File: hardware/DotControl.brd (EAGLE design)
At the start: 30.7 x 65 mm, 42 parts, among them CN1 1X4-BIG, J3 USB-MICROB, SW2 Previous, SW5 Previous, SW6 Next, SW8 Ok, U1 ATMEGA328P-MU-QFN32, U2 TMP102, U3 ATSHA204-TSU, U4 SI7021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

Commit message: Readjust R values for charger, add Spice link
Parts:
- R1: value 10Ω -> 75Ω
- R6: value 70Ω -> 1kΩ
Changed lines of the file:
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@@
 <element name="CN1" library="adafruit" package="1X04-BIG" value="1X4-BIG" x="11.2" y="9"/>
 <element name="SJ1" library="SparkFun" package="SJ_2S-TRACE" value="SOLDERJUMPERTRACE" x="16.7" y="26.4" rot="MR90"/>
-<element name="R1" library="resistor" package="R0603" value="10Ω" x="28.4226" y="60.5282" rot="MR270"/>
+<element name="R1" library="resistor" package="R0603" value="75Ω" x="28.4226" y="60.5282" rot="MR270"/>
 <element name="LED2" library="SparkFun" package="LED-0603" value="" x="27.4828" y="60.6044" rot="R180"/>
 <element name="U2" library="SparkFun" package="SOT563" value="TMP102" x="18.9992" y="13.1318" rot="MR270"/>
@@
 <element name="C8" library="resistor" package="C0603" value="0.1uF" x="9.8552" y="19.3548" rot="MR90"/>
 <element name="C4" library="resistor" package="C0603" value="0.1uF" x="3.1242" y="17.6022" rot="MR270"/>
-<element name="R6" library="resistor" package="R0603" value="70Ω" x="23.876" y="61.3918" rot="MR0"/>
+<element name="R6" library="resistor" package="R0603" value="1kΩ" x="23.876" y="61.3918" rot="MR0"/>
 <element name="C5" library="adafruit" package="C3216" value="100uF 4V" x="5.4864" y="21.0312" rot="R180"/>
 </elements>

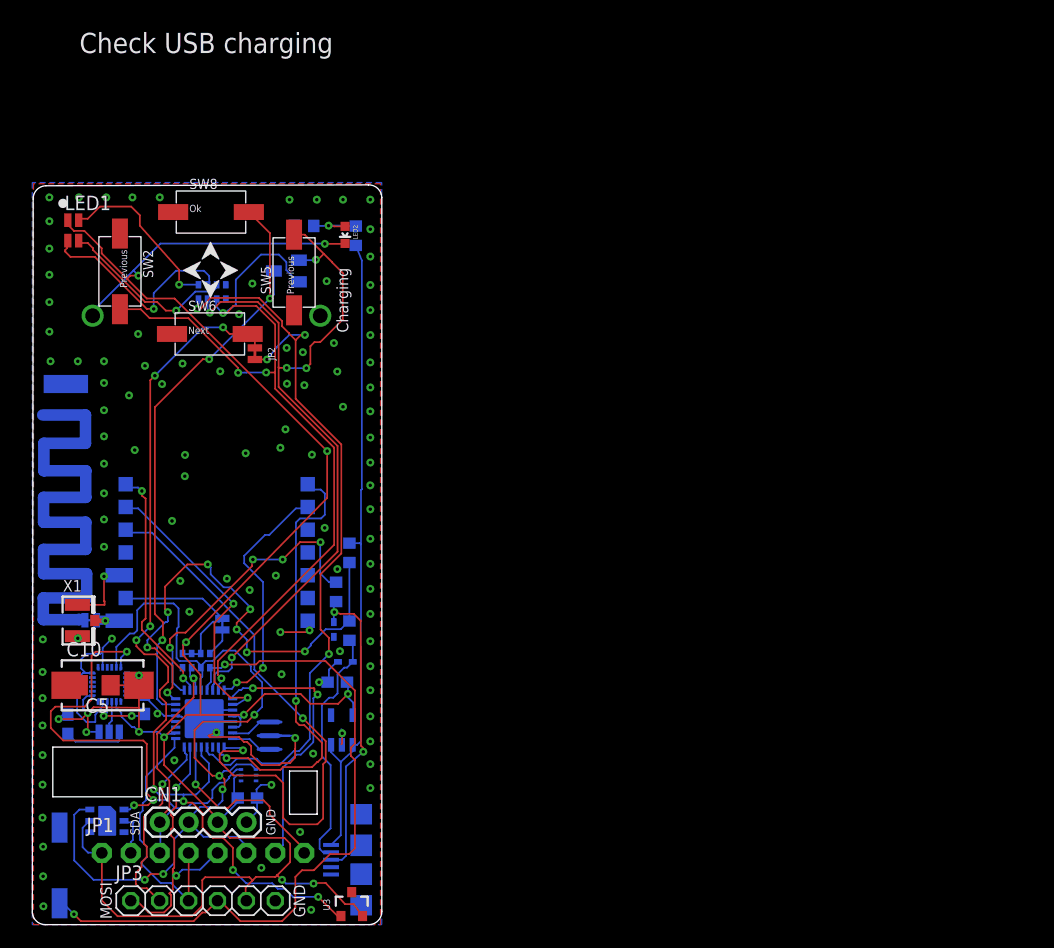
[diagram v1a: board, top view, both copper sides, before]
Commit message: Add pulldown on ENA pin of voltage reg to prefent 150uA quiescent current
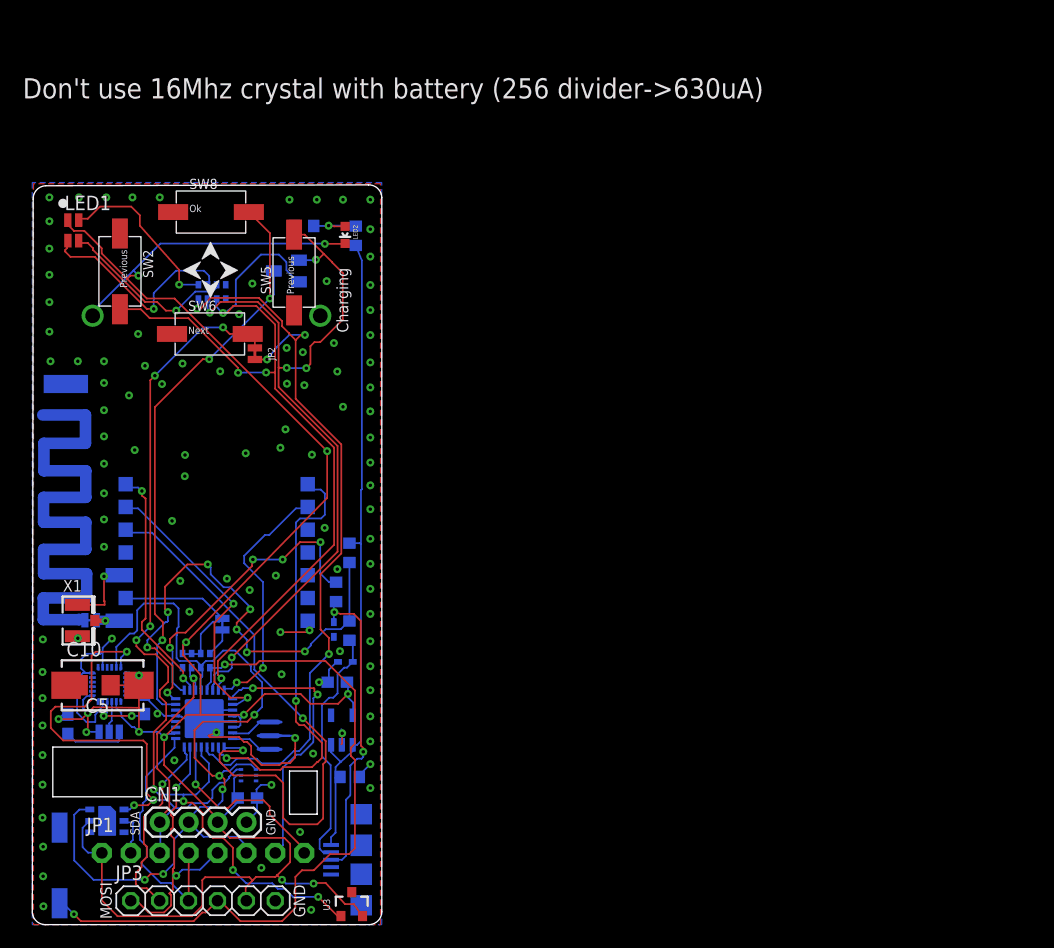
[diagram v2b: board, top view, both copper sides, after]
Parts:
- added R8: >1KΩ, resistor:R0603
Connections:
- net +5V: now also R8.2
- net GND: now also R8.1
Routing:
- net GND: track 79.4 -> 81.0 mm
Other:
- board text added: "Don't use 16Mhz crystal with battery (256 divider->630uA)"
- board text removed: "Check USB charging"
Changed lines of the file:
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@@
 <layer number="22" name="bPlace" color="7" fill="1" visible="yes" active="yes"/>
 <layer number="23" name="tOrigins" color="15" fill="1" visible="no" active="yes"/>
-<layer number="24" name="bOrigins" color="15" fill="1" visible="no" active="yes"/>
+<layer number="24" name="bOrigins" color="15" fill="1" visible="yes" active="yes"/>
 <layer number="25" name="tNames" color="7" fill="1" visible="no" active="yes"/>
 <layer number="26" name="bNames" color="7" fill="1" visible="no" active="yes"/>
@@
 <rectangle x1="0.1524" y1="25.527" x2="5.6388" y2="48.9204" layer="41"/>
 <rectangle x1="0.1524" y1="25.527" x2="5.6134" y2="48.9712" layer="42"/>
-<text x="4.1402" y="76.581" size="1.778" layer="21">Check USB charging</text>
 <text x="9.4234" y="7.8486" size="0.8128" layer="21" rot="R90">SDA</text>
 <text x="20.5486" y="10.16" size="0.8128" layer="21" rot="R270">GND</text>
+<text x="-0.8382" y="72.5932" size="1.778" layer="21">Don't use 16Mhz crystal with battery (256 divider-&gt;630uA)</text>
 </plain>
 <attributes>
@@
 <element name="R6" library="resistor" package="R0603" value="1kΩ" x="23.876" y="61.3918" rot="MR0"/>
 <element name="C5" library="adafruit" package="C3216" value="100uF 4V" x="5.4864" y="21.0312" rot="R180"/>
+<element name="R8" library="resistor" package="R0603" value="&gt;1KΩ" x="27.8892" y="12.9794" rot="MR0"/>
 </elements>
 <signals>
@@
 <wire x1="15.4432" y1="17.0372" x2="15.1" y2="17.0372" width="0.1524" layer="16"/>
 <wire x1="15.1" y1="17.0372" x2="15.1" y2="18.1" width="0.1524" layer="16"/>
+<contactref element="R8" pad="1"/>
+<wire x1="28.7392" y1="12.9794" x2="28.7392" y2="13.1392" width="0.1524" layer="16"/>
+<wire x1="28.7392" y1="13.1392" x2="29.7" y2="14.1" width="0.1524" layer="16"/>
 <wire x1="16.256" y1="17.85" x2="16.1798" y2="17.8308" width="0" layer="19" extent="16-16"/>
 </signal>
@@
 <wire x1="27.1018" y1="14.3002" x2="28.1686" y2="15.2654" width="0.1524" layer="16"/>
 <wire x1="28.1686" y1="15.2654" x2="28.15" y2="15.7999" width="0.1524" layer="16"/>
-<wire x1="27.1018" y1="14.3002" x2="27.1018" y2="7.8518" width="0.1524" layer="16"/>
-<wire x1="27.1018" y1="7.8518" x2="26.25" y2="7" width="0.1524" layer="16"/>
 <wire x1="27.8638" y1="33.5144" x2="28.7918" y2="33.5144" width="0.1524" layer="16"/>
 <wire x1="28.7918" y1="33.5144" x2="28.8798" y2="33.4264" width="0.1524" layer="16"/>
+<contactref element="R8" pad="2"/>
+<wire x1="26.25" y1="7" x2="26.25" y2="7.6826" width="0.1524" layer="16"/>
+<wire x1="26.25" y1="7.6826" x2="26.6446" y2="8.0772" width="0.1524" layer="16"/>
+<wire x1="26.6446" y1="8.0772" x2="26.6446" y2="12.9032" width="0.1524" layer="16"/>
+<wire x1="26.6446" y1="12.9032" x2="26.6446" y2="13.843" width="0.1524" layer="16"/>
+<wire x1="26.6446" y1="13.843" x2="27.1018" y2="14.3002" width="0.1524" layer="16"/>
+<wire x1="27.0392" y1="12.9794" x2="26.7208" y2="12.9794" width="0.1524" layer="16"/>
+<wire x1="26.7208" y1="12.9794" x2="26.6446" y2="12.9032" width="0.1524" layer="16"/>
 </signal>
 <signal name="MOSI">
@@
 <wire x1="26.25" y1="5.7" x2="27.2138" y2="5.7" width="0.1524" layer="16"/>
 <wire x1="27.2138" y1="5.7" x2="27.559" y2="6.0452" width="0.1524" layer="16"/>
-<wire x1="27.559" y1="6.0452" x2="27.559" y2="13.8938" width="0.1524" layer="16"/>
-<wire x1="27.559" y1="13.8938" x2="29.083" y2="15.1892" width="0.1524" layer="16"/>
 <wire x1="26.4922" y1="26.5842" x2="26.4922" y2="27.3558" width="0.1524" layer="16"/>
 <wire x1="26.4922" y1="27.3558" x2="26.4922" y2="28.1822" width="0.1524" layer="16"/>
@@
 <via x="26.543" y="27.4574" extent="1-16" drill="0.3"/>
 <wire x1="26.543" y1="27.4574" x2="26.4922" y2="27.3558" width="0.1524" layer="16"/>
+<wire x1="27.559" y1="6.0452" x2="27.559" y2="10.9728" width="0.1524" layer="16"/>
+<wire x1="27.559" y1="10.9728" x2="27.94" y2="11.3538" width="0.1524" layer="16"/>
+<wire x1="28.9814" y1="15.0876" x2="29.083" y2="15.1892" width="0.1524" layer="16"/>
+<wire x1="27.94" y1="11.3538" x2="27.94" y2="13.97" width="0.1524" layer="16"/>
+<wire x1="27.94" y1="13.97" x2="28.5496" y2="14.5796" width="0.1524" layer="16"/>
+<wire x1="28.5496" y1="14.5796" x2="28.9306" y2="14.5796" width="0.1524" layer="16"/>
+<wire x1="28.9306" y1="14.5796" x2="29.083" y2="14.732" width="0.1524" layer="16"/>
+<wire x1="29.083" y1="14.732" x2="29.083" y2="15.1892" width="0.1524" layer="16"/>
 </signal>
 <signal name="D-">

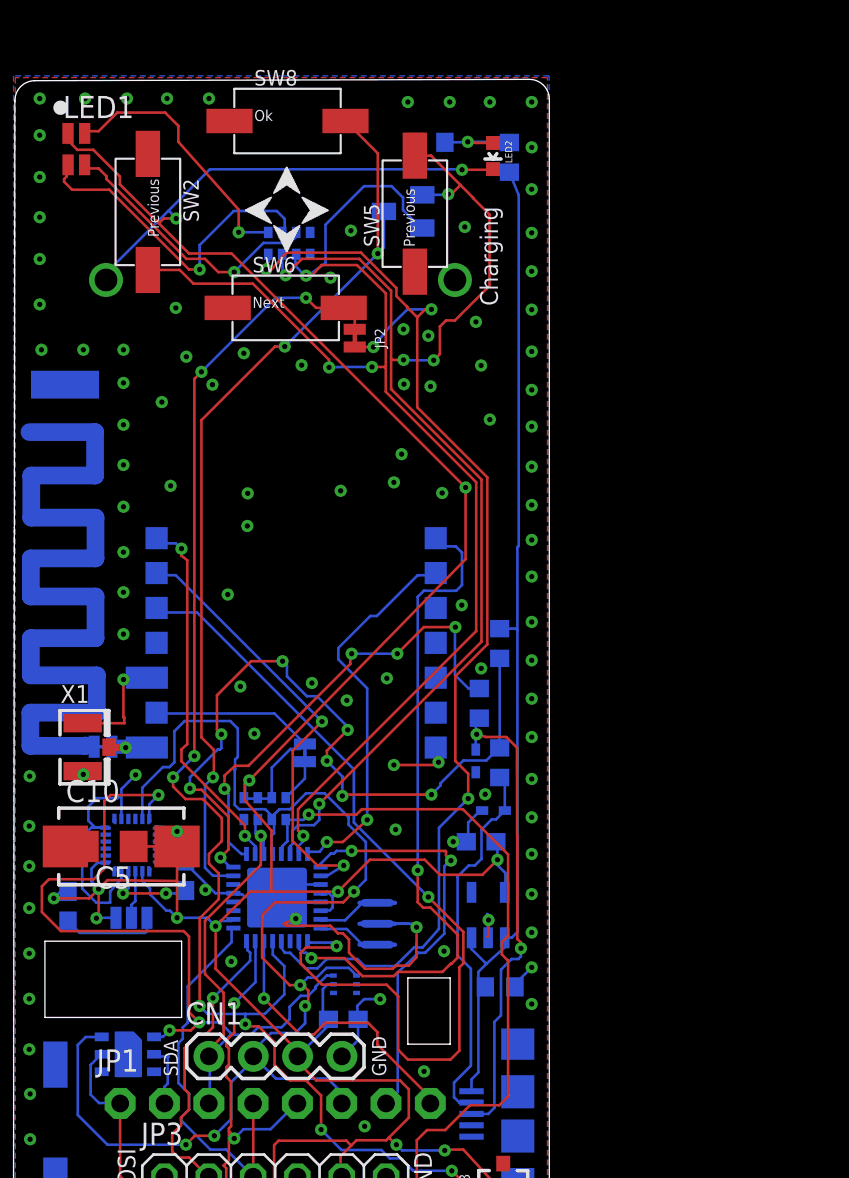
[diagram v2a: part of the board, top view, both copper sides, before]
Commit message: [Intermediate] Improve coincell charging
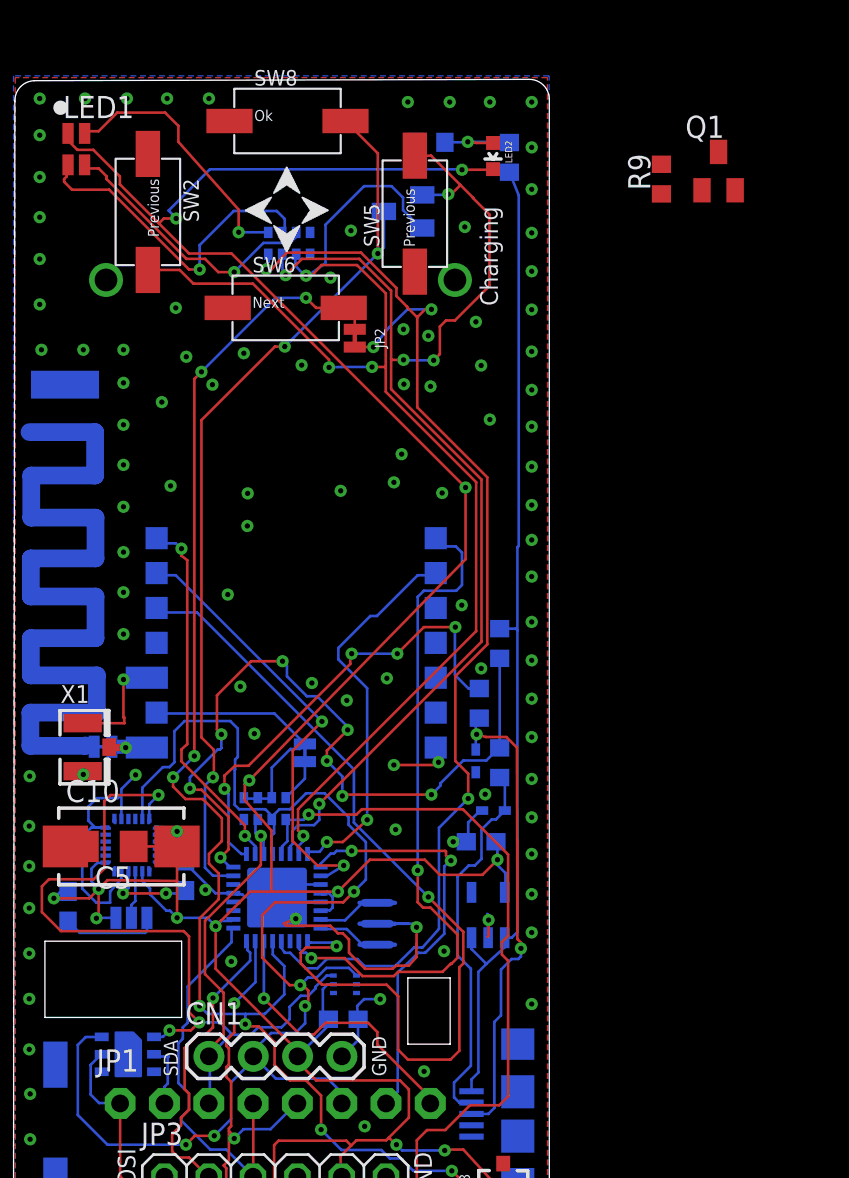
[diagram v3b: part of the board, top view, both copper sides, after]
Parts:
- removed R8: >1KΩ, resistor:R0603
- added Q1: (no value), adafruit:SOT23
- added R9: >1kΩ, resistor:R0603
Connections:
- new net N$18: BAT1.1, LED2.C, Q1.2
- net +3V3: now also Q1.3; no longer BAT1.1, LED2.C
- net +5V: now also Q1.1, R9.2; no longer R8.2
- net GND: now also R9.1; no longer R8.1
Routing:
- net +3V3: track 223.1 -> 217.6 mm
- net GND: track 81.0 -> 79.4 mm, vias 106 -> 105
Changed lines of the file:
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@@
 <layer number="21" name="tPlace" color="7" fill="1" visible="yes" active="yes"/>
 <layer number="22" name="bPlace" color="7" fill="1" visible="yes" active="yes"/>
-<layer number="23" name="tOrigins" color="15" fill="1" visible="no" active="yes"/>
+<layer number="23" name="tOrigins" color="15" fill="1" visible="yes" active="yes"/>
 <layer number="24" name="bOrigins" color="15" fill="1" visible="yes" active="yes"/>
 <layer number="25" name="tNames" color="7" fill="1" visible="no" active="yes"/>
@@
 <element name="R6" library="resistor" package="R0603" value="1kΩ" x="23.876" y="61.3918" rot="MR0"/>
 <element name="C5" library="adafruit" package="C3216" value="100uF 4V" x="5.4864" y="21.0312" rot="R180"/>
-<element name="R8" library="resistor" package="R0603" value="&gt;1KΩ" x="27.8892" y="12.9794" rot="MR0"/>
+<element name="R9" library="resistor" package="R0603" value="&gt;1kΩ" x="37.1348" y="59.2836" rot="R90"/>
+<element name="Q1" library="adafruit" package="SOT23" value="" x="40.4114" y="59.7408"/>
 </elements>
 <signals>
@@
 <contactref element="SW1" pad="2"/>
 <via x="29.7" y="12" extent="1-16" drill="0.3"/>
-<via x="29.7" y="14.1" extent="1-16" drill="0.3"/>
 <via x="29.7" y="16.1" extent="1-16" drill="0.3"/>
 <via x="29.7" y="18.3" extent="1-16" drill="0.3"/>
@@
 <wire x1="15.4432" y1="17.0372" x2="15.1" y2="17.0372" width="0.1524" layer="16"/>
 <wire x1="15.1" y1="17.0372" x2="15.1" y2="18.1" width="0.1524" layer="16"/>
-<contactref element="R8" pad="1"/>
-<wire x1="28.7392" y1="12.9794" x2="28.7392" y2="13.1392" width="0.1524" layer="16"/>
-<wire x1="28.7392" y1="13.1392" x2="29.7" y2="14.1" width="0.1524" layer="16"/>
-<wire x1="16.256" y1="17.85" x2="16.1798" y2="17.8308" width="0" layer="19" extent="16-16"/>
+<contactref element="R9" pad="1"/>
+<wire x1="29.7" y1="58.7" x2="37.1348" y2="58.4336" width="0" layer="19" extent="1-1"/>
+<wire x1="16.1798" y1="17.8308" x2="16.256" y2="17.85" width="0" layer="19" extent="16-16"/>
 </signal>
 <signal name="SCK">
@@
 <wire x1="27.4828" y1="1.8034" x2="28.2456" y2="1.8034" width="0.1524" layer="1"/>
 <wire x1="28.2456" y1="1.8034" x2="29.017" y2="0.7526" width="0.1524" layer="1"/>
-<contactref element="LED2" pad="C"/>
-<contactref element="BAT1" pad="1"/>
-<wire x1="5.3" y1="53.5" x2="5.3" y2="53.8902" width="0.1524" layer="16"/>
-<wire x1="5.3" y1="53.8902" x2="8.89" y2="57.4802" width="0.1524" layer="16"/>
 <wire x1="8.89" y1="57.4802" x2="11.2522" y2="59.8424" width="0.1524" layer="16"/>
 <wire x1="11.2522" y1="59.8424" x2="25.6794" y2="59.8424" width="0.1524" layer="16"/>
@@
 <via x="25.7048" y="59.817" extent="1-16" drill="0.3"/>
 <wire x1="25.7048" y1="59.817" x2="27.4454" y2="59.817" width="0.1524" layer="1"/>
-<wire x1="27.4454" y1="59.817" x2="27.4828" y2="59.8544" width="0.1524" layer="1"/>
 <via x="9.3218" y="57.023" extent="1-16" drill="0.3"/>
 <wire x1="9.3218" y1="57.023" x2="9.3218" y2="57.0484" width="0.1524" layer="16"/>
@@
 <wire x1="8.763" y1="17.3482" x2="8.9662" y2="17.3482" width="0.1524" layer="16"/>
 <wire x1="8.9662" y1="17.3482" x2="9.3726" y2="16.9418" width="0.1524" layer="16"/>
+<contactref element="Q1" pad="3"/>
+<wire x1="27.4454" y1="59.817" x2="40.4114" y2="60.8408" width="0" layer="19" extent="1-1"/>
 </signal>
 <signal name="PUSH">
@@
 <wire x1="27.8638" y1="33.5144" x2="28.7918" y2="33.5144" width="0.1524" layer="16"/>
 <wire x1="28.7918" y1="33.5144" x2="28.8798" y2="33.4264" width="0.1524" layer="16"/>
-<contactref element="R8" pad="2"/>
 <wire x1="26.25" y1="7" x2="26.25" y2="7.6826" width="0.1524" layer="16"/>
 <wire x1="26.25" y1="7.6826" x2="26.6446" y2="8.0772" width="0.1524" layer="16"/>
-<wire x1="26.6446" y1="8.0772" x2="26.6446" y2="12.9032" width="0.1524" layer="16"/>
-<wire x1="26.6446" y1="12.9032" x2="26.6446" y2="13.843" width="0.1524" layer="16"/>
+<wire x1="26.6446" y1="8.0772" x2="26.6446" y2="13.843" width="0.1524" layer="16"/>
 <wire x1="26.6446" y1="13.843" x2="27.1018" y2="14.3002" width="0.1524" layer="16"/>
-<wire x1="27.0392" y1="12.9794" x2="26.7208" y2="12.9794" width="0.1524" layer="16"/>
-<wire x1="26.7208" y1="12.9794" x2="26.6446" y2="12.9032" width="0.1524" layer="16"/>
+<contactref element="R9" pad="2"/>
+<contactref element="Q1" pad="1"/>
+<wire x1="37.1348" y1="60.1336" x2="39.4614" y2="58.6408" width="0" layer="19" extent="1-1"/>
+<wire x1="28.956" y1="58.3574" x2="37.1348" y2="60.1336" width="0" layer="19" extent="1-16"/>
 </signal>
 <signal name="MOSI">
@@
 <wire x1="9.6892" y1="18.3388" x2="9.8552" y2="18.5048" width="0.1524" layer="16"/>
 </signal>
+<signal name="N$18">
+<contactref element="LED2" pad="C"/>
+<contactref element="BAT1" pad="1"/>
+<contactref element="Q1" pad="2"/>
+<wire x1="27.4828" y1="59.8544" x2="41.3614" y2="58.6408" width="0" layer="19" extent="1-1"/>
+<wire x1="5.3" y1="53.5" x2="27.4828" y2="59.8544" width="0" layer="19" extent="1-1"/>
+</signal>
 </signals>
